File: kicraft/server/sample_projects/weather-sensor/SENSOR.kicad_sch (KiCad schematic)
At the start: 2 parts, among them U3 BMP280

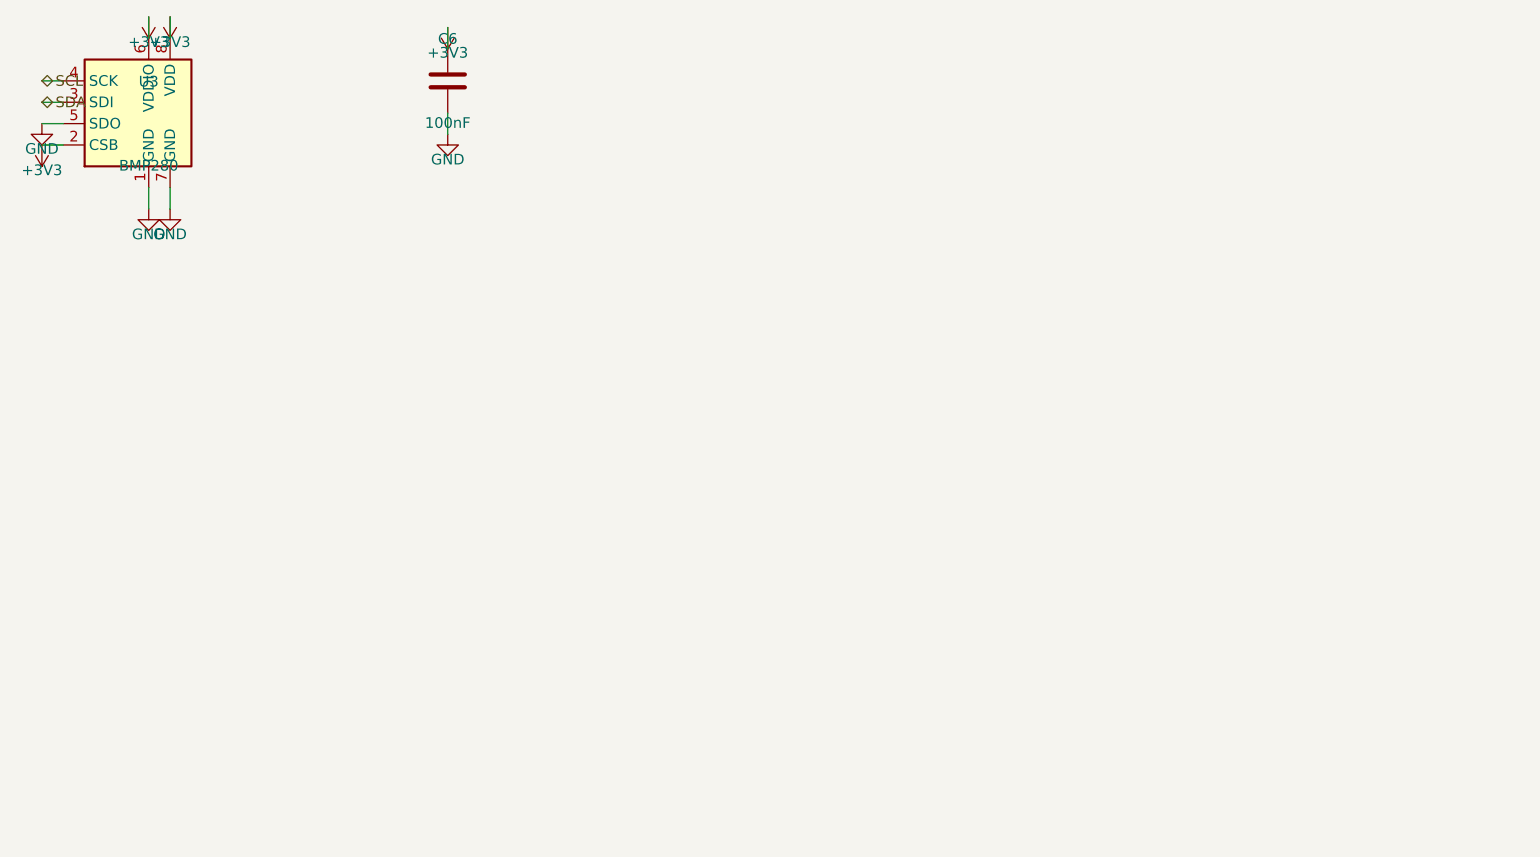
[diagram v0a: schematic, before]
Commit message: feat(web): refresh showcase samples from self-eval, add interactive 3D models
Replace the three landing-page showcase boards (motion-sensor, weather-sensor,
led-matrix) with the top three boards from self-eval batch 20260613T034718Z —
all grade B, fab-ready (build_rc=0), no gates:

  - weather-sensor  BMP280 Qwiic sensor     final 83.0  (featured)
  - bench-breakout  USB-C 3.3V/5V rails     final 79.0
  - night-light     PIR + warm-white LEDs   final 78.5

The hero and gallery now show interactive, rotatable 3D models (a
<model-viewer> of each board's board.glb) instead of a static image, with the
rendered board.png as the poster / no-JS fallback. A sample without a GLB
degrades to exactly the old <img>. model-viewer 4.0.0 (BSD-3) is self-hosted
in static/ like kicanvas.js, so there is no CDN runtime dependency.

Promotion is scripted (scripts/promote_to_sample.py): it copies the curated
KiCad tree, stages each bundle library's 3D models under 3dmodels/, and
rewrites the routed board's broken bundle model refs (a bare /X.wrl that
resolves nowhere) to ${KIPRJMOD}/3dmodels/<lib>/X.wrl so kicad-cli renders
component bodies, then renders a transparent-background board.png and exports
board.glb.

Co-Authored-By: Claude Opus 4.8 (1M context) <noreply@anthropic.com>
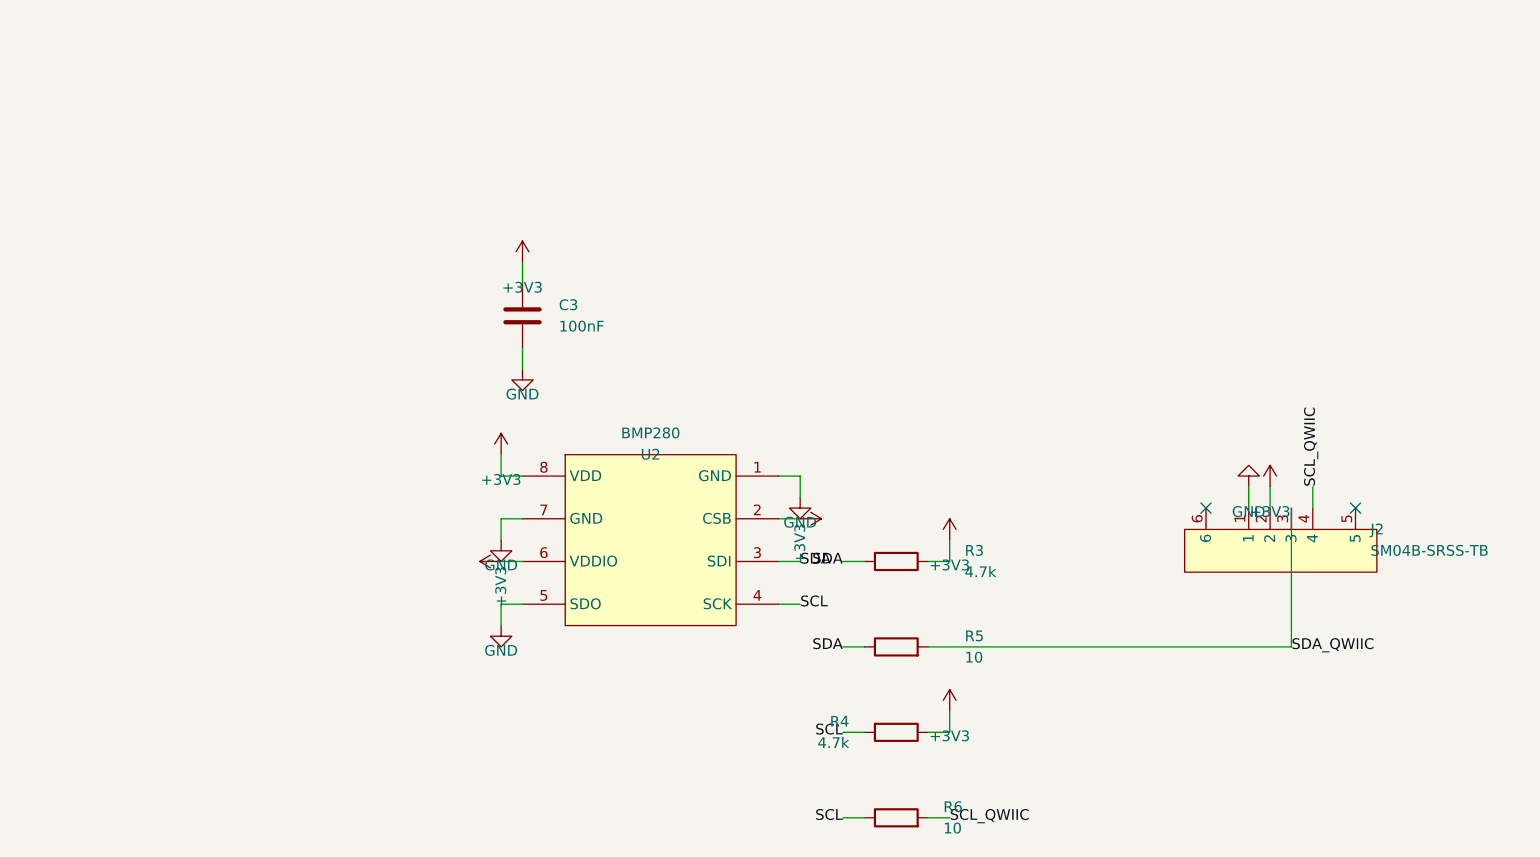
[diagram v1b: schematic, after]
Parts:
- removed C6: 100nF, Capacitor_SMD:C_0402_1005Metric, symbol Device:C
- removed U3: BMP280, Package_LGA:Bosch_LGA-8_2x2.5mm_P0.65mm_ClockwisePinNumbering, symbol Sensor_Pressure:BMP280
- added C3: 100nF, Capacitor_SMD:C_0805_2012Metric, symbol Device:C
- added J2: SM04B-SRSS-TB, jst-sh-4p-qwiic:CONN-SMD_4P-P1.00_SM04B-SRSS-TB-LF-SN, symbol jst-sh-4p-qwiic:SM04B-SRSS-TB
- added R3, R4: 4.7k, Resistor_SMD:R_0805_2012Metric, symbol Device:R
- added R5, R6: 10, Resistor_SMD:R_0805_2012Metric, symbol Device:R
- added U2: BMP280, bmp280-bosch-sensor:LGA-8_L2.5-W2.0-P0.65_AMP6127, symbol bmp280-bosch-sensor:BMP280
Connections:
- net +3V3: now also C3.1, J2.2, R3.1, R4.1, U2.2 (CSB), U2.6 (VDDIO), U2.8 (VDD)
- net GND: now also C3.2, J2.1, U2.1 (GND), U2.5 (SDO), U2.7 (GND)
- net SCL: now also R4.2, R6.1, U2.4 (SCK)
- net SDA: now also R3.2, R5.1, U2.3 (SDI)
- new net SCL_QWIIC: J2.4, R6.2
- new net SDA_QWIIC: J2.3, R5.2
- no-connect marks 0 -> 2

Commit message: feat(showcase): refresh landing samples from self-eval 20260614
Promote the three best boards from self-eval batch 20260614T215540Z
(all grade B) into the landing-page showcase, replacing the regressed
PIR night light (D/45, hit erc_errors + unprogrammable_mcu gates):

- usb-pd-trigger (NEW, featured hero) — 81.0, fab-ready
- weather-sensor (re-promoted; stem A_BMP280_BAROMETRIC -> BMP280_QWIIC_USB_C)
- bench-breakout (re-promoted; 4->5 sheets, 16->19 parts)

Regenerated board.png/hero.png renders and interactive board.glb models
via scripts/promote_to_sample.py. Already live (deploy/restart-web.sh).

Co-Authored-By: Claude Opus 4.8 (1M context) <noreply@anthropic.com>
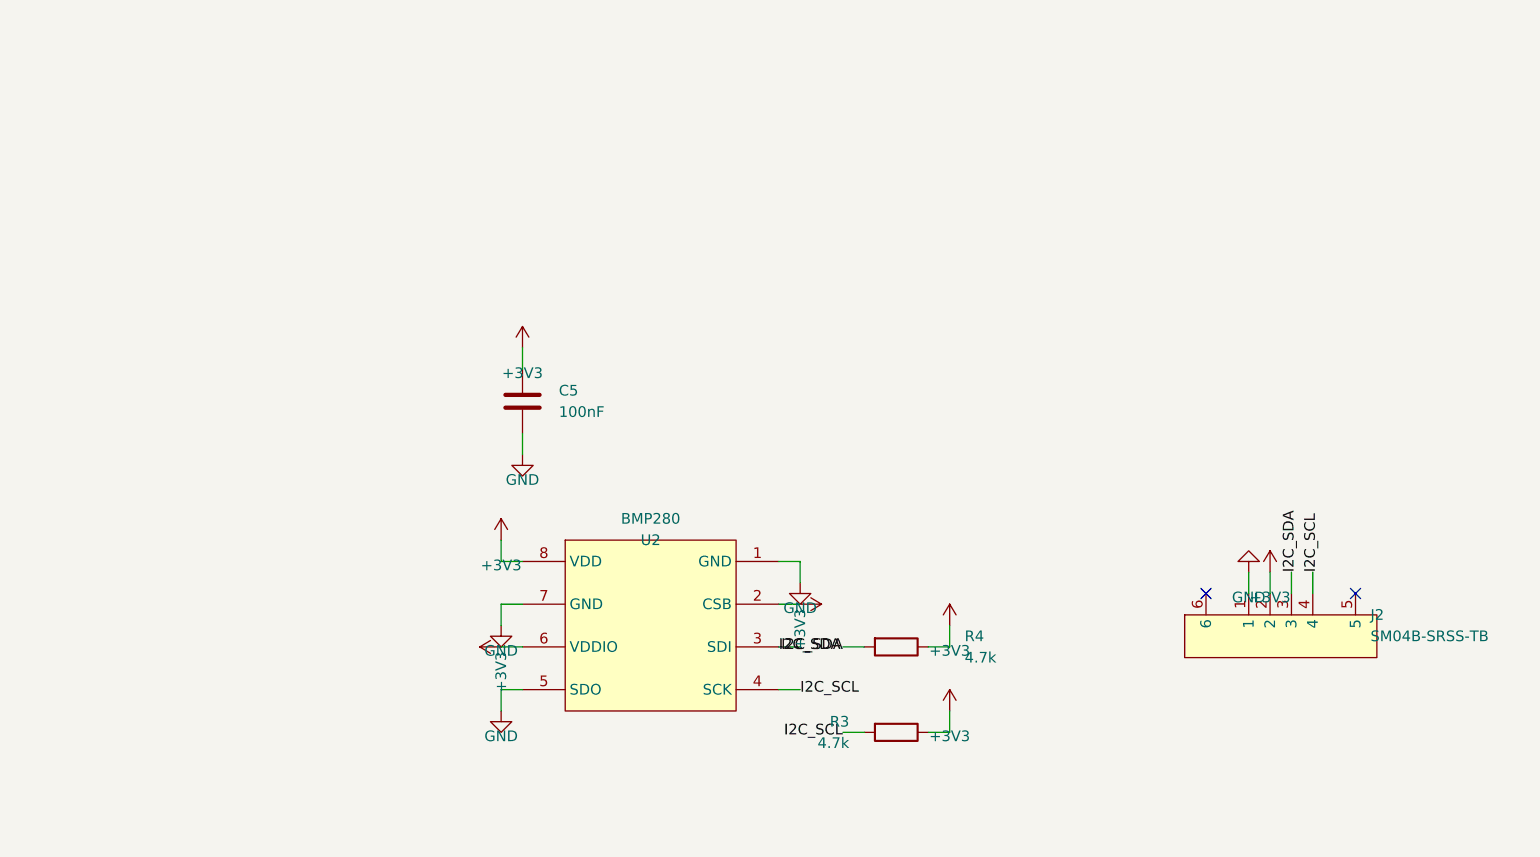
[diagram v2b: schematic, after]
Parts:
- removed C3: 100nF, Capacitor_SMD:C_0805_2012Metric, symbol Device:C
- removed R5, R6: 10, Resistor_SMD:R_0805_2012Metric, symbol Device:R
- added C5: 100nF, Capacitor_SMD:C_0805_2012Metric, symbol Device:C
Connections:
- net SCL_QWIIC is gone; now on net I2C_SCL: J2.4
- net SDA_QWIIC is gone; now on net I2C_SDA: J2.3
- net +3V3: now also C5.1
- net GND: now also C5.2
- net SCL renamed I2C_SCL
- net I2C_SCL: now also R3.2; no longer R4.2
- net SDA renamed I2C_SDA
- net I2C_SDA: now also R4.2; no longer R3.2
